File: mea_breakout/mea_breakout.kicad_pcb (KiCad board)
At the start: 2 copper layers, 67 x 67 mm, 502 parts, among them J1 Conn_01x01_Male, J10 Conn_01x01_Male, J100 Conn_01x01_Male, J101 Conn_01x01_Male, J102 Conn_01x01_Male, J103 Conn_01x01_Male, J104 Conn_01x01_Male, J105 Conn_01x01_Male, J106 Conn_01x01_Male, J107 Conn_01x01_Male, J108 Conn_01x01_Male, J109 Conn_01x01_Male, J11 Conn_01x01_Male, J110 Conn_01x01_Male, J111 Conn_01x01_Male, J112 Conn_01x01_Male, J113 Conn_01x01_Male, J114 Conn_01x01_Male, J115 Conn_01x01_Male, J116 Conn_01x01_Male, J117 Conn_01x01_Male, J118 Conn_01x01_Male, J119 Conn_01x01_Male, J12 Conn_01x01_Male, J120 Conn_01x01_Male, J121 Conn_01x01_Male, J122 Conn_01x01_Male, J123 Conn_01x01_Male, J124 Conn_01x01_Male, J125 Conn_01x01_Male, J126 Conn_01x01_Male, J127 Conn_01x01_Male, J128 Conn_01x01_Male, J129 Conn_01x01_Male, J13 Conn_01x01_Male, J130 Conn_01x01_Male, J131 Conn_01x01_Male, J132 Conn_01x01_Male, J134 Conn_01x01_Male, J135 Conn_01x01_Male, J136 Conn_01x01_Male, J137 Conn_01x01_Male, J138 Conn_01x01_Male, J139 Conn_01x01_Male, J14 Conn_01x01_Male, J140 Conn_01x01_Male, J141 Conn_01x01_Male, J142 Conn_01x01_Male, J143 Conn_01x01_Male, J144 Conn_01x01_Male, J145 Conn_01x01_Male, J146 Conn_01x01_Male, J147 Conn_01x01_Male, J148 Conn_01x01_Male, J149 Conn_01x01_Male, J15 Conn_01x01_Male, J150 Conn_01x01_Male, J151 Conn_01x01_Male, J152 Conn_01x01_Male, J153 Conn_01x01_Male, J154 Conn_01x01_Male, J155 Conn_01x01_Male, J156 Conn_01x01_Male, J157 Conn_01x01_Male, J158 Conn_01x01_Male, J159 Conn_01x01_Male, J16 Conn_01x01_Male, J160 Conn_01x01_Male, J161 Conn_01x01_Male, J163 Conn_01x01_Male, J164 Conn_01x01_Male, J165 Conn_01x01_Male, J166 Conn_01x01_Male, J167 Conn_01x01_Male, J168 Conn_01x01_Male, J169 Conn_01x01_Male, J17 Conn_01x01_Male, J170 Conn_01x01_Male, J171 Conn_01x01_Male, J172 Conn_01x01_Male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

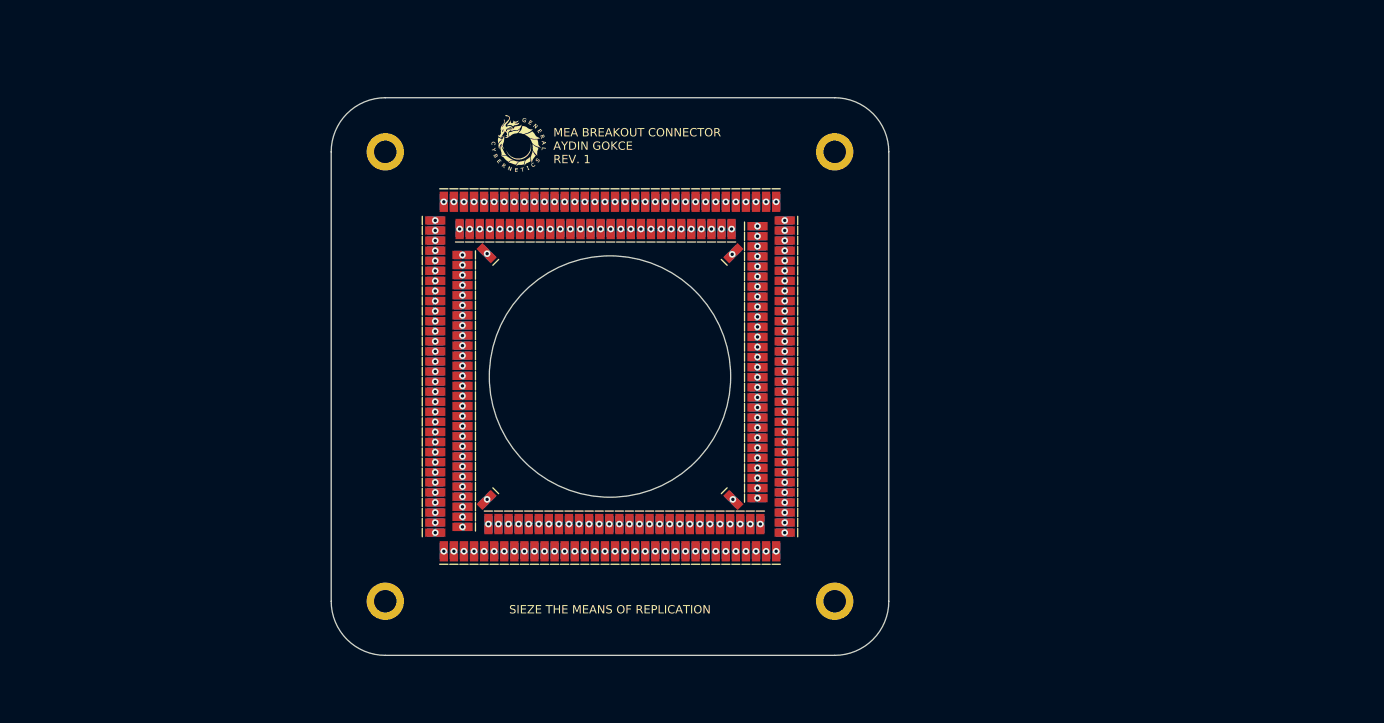
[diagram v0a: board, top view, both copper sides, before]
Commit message: fix: removed soldermask covering pads, lay rows out in the correct square shape
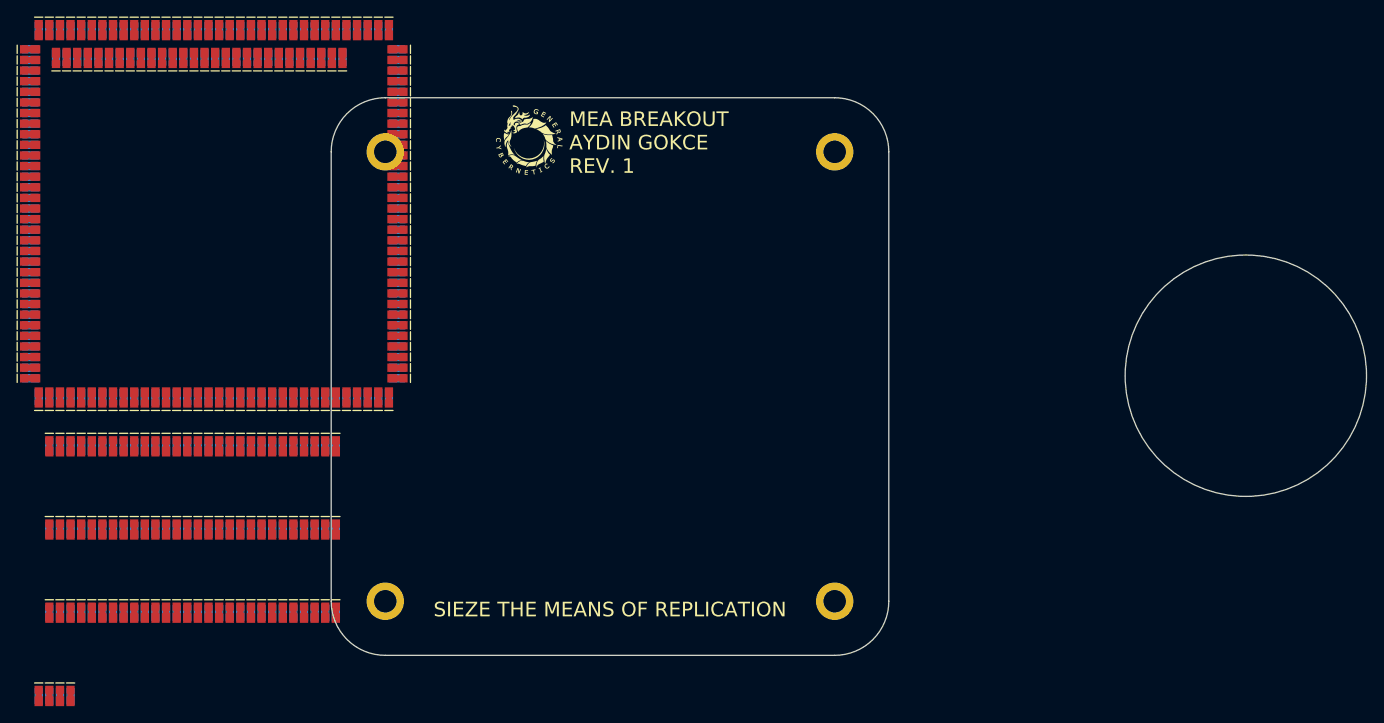
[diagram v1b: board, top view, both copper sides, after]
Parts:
- removed the G*** at (57.6, 12.7)
- removed the G*** at (79.7, 12.7)
- added G***: LOGO, LOGO, F.Cu at (58.9, 12.2)
- J1, J10, J100, J101, J102, J103, J104, J105, J106, J107, J108, J109, J11, J110, J111, J112, J113, J114, J115, J116, J117, J118, J119, J12, J120, J121, J122, J123, J124, J125, J126, J127, J128, J129, J13, J130, J131, J132, J134, J135, J136, J137, J138, J139, J14, J140, J141, J142, J143, J144, J145, J146, J147, J148, J149, J15, J150, J151, J152, J153, J154, J155, J156, J157, J158, J159, J16, J160, J161, J163, J164, J165, J166, J167, J168, J169, J17, J170, J171, J172, J173, J174, J175, J176, J177, J178, J179, J18, J180, J181, J182, J183, J184, J185, J186, J187, J188, J189, J19, J190, J192, J193, J194, J195, J196, J197, J198, J199, J2, J20, J200, J201, J202, J203, J204, J205, J206, J207, J208, J209, J21, J210, J211, J212, J213, J214, J215, J216, J217, J218, J219, J22, J221, J222, J223, J224, J225, J226, J227, J228, J229, J23, J230, J231, J232, J233, J234, J235, J236, J237, J238, J239, J24, J240, J241, J242, J243, J244, J245, J246, J247, J248, J249, J25, J250, J251, J252, J26, J27, J28, J29, J3, J30, J31, J32, J33, J34, J35, J36, J37, J38, J39, J4, J40, J41, J42, J43, J44, J45, J46, J47, J48, J49, J5, J50, J51, J52, J53, J54, J55, J56, J57, J58, J59, J6, J60, J61, J62, J63, J64, J65, J66, J67, J68, J69, J7, J70, J71, J72, J73, J74, J75, J76, J77, J78, J79, J8, J80, J81, J82, J83, J84, J85, J86, J87, J88, J89, J9, J90, J91, J92, J93, J94, J95, J96, J97, J98, J99: footprint 1mm_x_1mm_solder_pad:1mm_x_1mm_solder_pad -> 1mm_x_1mm_solder_pad
- U1, U10, U100, U101, U102, U103, U104, U105, U106, U107, U108, U109, U11, U110, U111, U112, U113, U114, U115, U116, U117, U118, U119, U12, U120, U121, U122, U123, U124, U125, U126, U127, U128, U129, U13, U130, U131, U132, U134, U135, U136, U137, U138, U139, U14, U140, U141, U142, U143, U144, U145, U146, U147, U148, U149, U15, U150, U151, U152, U153, U154, U155, U156, U157, U158, U159, U16, U160, U161, U163, U164, U165, U166, U167, U168, U169, U17, U170, U171, U172, U173, U174, U175, U176, U177, U178, U179, U18, U180, U181, U182, U183, U184, U185, U186, U187, U188, U189, U19, U190, U192, U193, U194, U195, U196, U197, U198, U199, U2, U20, U200, U201, U202, U203, U204, U205, U206, U207, U208, U209, U21, U210, U211, U212, U213, U214, U215, U216, U217, U218, U219, U22, U221, U222, U223, U224, U225, U226, U227, U228, U229, U23, U230, U231, U232, U233, U234, U235, U236, U237, U238, U239, U24, U240, U241, U242, U243, U244, U245, U246, U247, U248, U249, U25, U250, U251, U252, U26, U27, U28, U29, U3, U30, U31, U32, U33, U34, U35, U36, U37, U38, U39, U4, U40, U41, U42, U43, U44, U45, U46, U47, U48, U49, U5, U50, U51, U52, U53, U54, U55, U56, U57, U58, U59, U6, U60, U61, U62, U63, U64, U65, U66, U67, U68, U69, U7, U70, U71, U72, U73, U74, U75, U76, U77, U78, U79, U8, U80, U81, U82, U83, U84, U85, U86, U87, U88, U89, U9, U90, U91, U92, U93, U94, U95, U96, U97, U98, U99: footprint TE_2329497-2:TE_2329497-2 -> TE_2329497-2
- moved U1 107.3 mm to (0.00, 0.00), turned to 90 degrees
- moved U2 105.3 mm to (1.27, 0.00), turned to 90 degrees
- moved U3 103.3 mm to (2.55, 0.00), turned to 90 degrees
- moved J134 102.6 mm to (2.08, 1.27), turned to -90 degrees
- moved U4 101.3 mm to (3.82, 0.00), turned to 90 degrees
- moved J135 100.6 mm to (3.35, 1.27), turned to -90 degrees
- moved U250 99.5 mm to (1.27, 80.0), turned to 90 degrees
- moved U5 99.3 mm to (5.10, 0.00), turned to 90 degrees
- moved J250 98.8 mm to (1.27, 80.0), turned to 90 degrees
- moved J136 98.6 mm to (4.62, 1.27), turned to -90 degrees
- moved U6 97.3 mm to (6.38, 0.00), turned to 90 degrees
- moved J137 96.6 mm to (5.90, 1.27), turned to -90 degrees
- moved U7 95.4 mm to (7.65, 0.00), turned to 90 degrees
- moved J138 94.6 mm to (7.17, 1.27), turned to -90 degrees
- moved U8 93.5 mm to (8.92, 0.00), turned to 90 degrees
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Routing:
- net (no net): vias 248 -> 0
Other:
- board size 67 x 67 mm -> 124.4 x 67 mm
- board text added: "MEA BREAKOUT AYDIN GOKCE REV. 1"
- board text removed: "MEA BREAKOUT CONNECTOR AYDIN GOKCE REV. 1"

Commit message: changed soldermask to black, exported step files
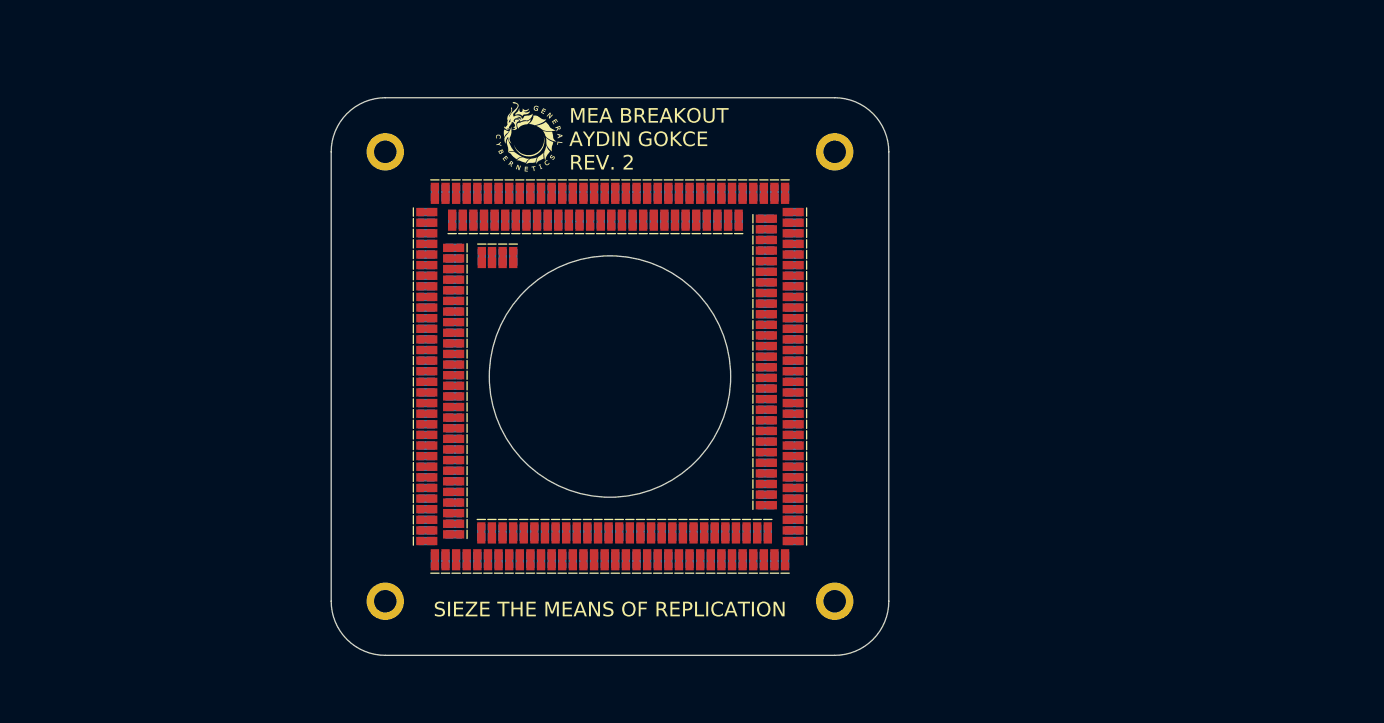
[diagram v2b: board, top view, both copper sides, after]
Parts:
- added G***: LOGO, LOGO, F.Cu at (58.9, 11.8)
- G***: moved to B.Cu
- J1, J10, J100, J101, J102, J103, J104, J105, J106, J107, J108, J109, J11, J110, J111, J112, J113, J114, J115, J116, J117, J118, J119, J12, J120, J121, J122, J123, J124, J125, J126, J127, J128, J129, J13, J130, J131, J132, J134, J135, J136, J137, J138, J139, J14, J140, J141, J142, J143, J144, J145, J146, J147, J148, J149, J15, J150, J151, J152, J153, J154, J155, J156, J157, J158, J159, J16, J160, J161, J163, J164, J165, J166, J167, J168, J169, J17, J170, J171, J172, J173, J174, J175, J176, J177, J178, J179, J18, J180, J181, J182, J183, J184, J185, J186, J187, J188, J189, J19, J190, J192, J193, J194, J195, J196, J197, J198, J199, J2, J20, J200, J201, J202, J203, J204, J205, J206, J207, J208, J209, J21, J210, J211, J212, J213, J214, J215, J216, J217, J218, J219, J22, J221, J222, J223, J224, J225, J226, J227, J228, J229, J23, J230, J231, J232, J233, J234, J235, J236, J237, J238, J239, J24, J240, J241, J242, J243, J244, J245, J246, J247, J248, J249, J25, J250, J251, J252, J26, J27, J28, J29, J3, J30, J31, J32, J33, J34, J35, J36, J37, J38, J39, J4, J40, J41, J42, J43, J44, J45, J46, J47, J48, J49, J5, J50, J51, J52, J53, J54, J55, J56, J57, J58, J59, J6, J60, J61, J62, J63, J64, J65, J66, J67, J68, J69, J7, J70, J71, J72, J73, J74, J75, J76, J77, J78, J79, J8, J80, J81, J82, J83, J84, J85, J86, J87, J88, J89, J9, J90, J91, J92, J93, J94, J95, J96, J97, J98, J99: footprint 1mm_x_1mm_solder_pad -> 1mm_x_1mm_solder_pad:1mm_x_1mm_solder_pad
- U1, U10, U100, U101, U102, U103, U104, U105, U106, U107, U108, U109, U11, U110, U111, U112, U113, U114, U115, U116, U117, U118, U119, U12, U120, U121, U122, U123, U124, U125, U126, U127, U128, U129, U13, U130, U131, U132, U134, U135, U136, U137, U138, U139, U14, U140, U141, U142, U143, U144, U145, U146, U147, U148, U149, U15, U150, U151, U152, U153, U154, U155, U156, U157, U158, U159, U16, U160, U161, U163, U164, U165, U166, U167, U168, U169, U17, U170, U171, U172, U173, U174, U175, U176, U177, U178, U179, U18, U180, U181, U182, U183, U184, U185, U186, U187, U188, U189, U19, U190, U192, U193, U194, U195, U196, U197, U198, U199, U2, U20, U200, U201, U202, U203, U204, U205, U206, U207, U208, U209, U21, U210, U211, U212, U213, U214, U215, U216, U217, U218, U219, U22, U221, U222, U223, U224, U225, U226, U227, U228, U229, U23, U230, U231, U232, U233, U234, U235, U236, U237, U238, U239, U24, U240, U241, U242, U243, U244, U245, U246, U247, U248, U249, U25, U250, U251, U252, U26, U27, U28, U29, U3, U30, U31, U32, U33, U34, U35, U36, U37, U38, U39, U4, U40, U41, U42, U43, U44, U45, U46, U47, U48, U49, U5, U50, U51, U52, U53, U54, U55, U56, U57, U58, U59, U6, U60, U61, U62, U63, U64, U65, U66, U67, U68, U69, U7, U70, U71, U72, U73, U74, U75, U76, U77, U78, U79, U8, U80, U81, U82, U83, U84, U85, U86, U87, U88, U89, U9, U90, U91, U92, U93, U94, U95, U96, U97, U98, U99: footprint TE_2329497-2 -> TE_2329497-2:TE_2329497-2
- moved J221 99.7 mm to (88.4, 21.6), turned to 180 degrees
- moved U221 99.7 mm to (88.4, 21.6), turned to 180 degrees
- moved J222 97.9 mm to (88.4, 22.9), turned to 180 degrees
- moved U222 97.9 mm to (88.4, 22.9), turned to 180 degrees
- moved J223 96.2 mm to (88.4, 24.2), turned to 180 degrees
- moved U223 96.2 mm to (88.4, 24.2), turned to 180 degrees
- moved J224 94.5 mm to (88.4, 25.5), turned to 180 degrees
- moved U224 94.5 mm to (88.4, 25.5), turned to 180 degrees
- moved J225 92.7 mm to (88.4, 26.7), turned to 180 degrees
- moved U225 92.7 mm to (88.4, 26.7), turned to 180 degrees
- moved J226 91.0 mm to (88.4, 28.0), turned to 180 degrees
- moved U226 91.0 mm to (88.4, 28.0), turned to 180 degrees
- moved J227 89.3 mm to (88.4, 29.3), turned to 180 degrees
- moved U227 89.3 mm to (88.4, 29.3), turned to 180 degrees
- moved J228 87.6 mm to (88.4, 30.6), turned to 180 degrees
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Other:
- board size 124.4 x 67 mm -> 67 x 67 mm
- board text added: "MEA BREAKOUT AYDIN GOKCE REV. 2"
- board text removed: "MEA BREAKOUT AYDIN GOKCE REV. 1"
